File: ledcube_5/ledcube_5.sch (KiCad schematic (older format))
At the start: 60 parts, among them Q1 PN2222A, Q2 PN2222A, Q3 PN2222A, Q4 PN2222A, Q5 PN2222A, U1 74HC595, U2 74HC595, U3 74HC595, U4 74HC595, U5 FE310-G000

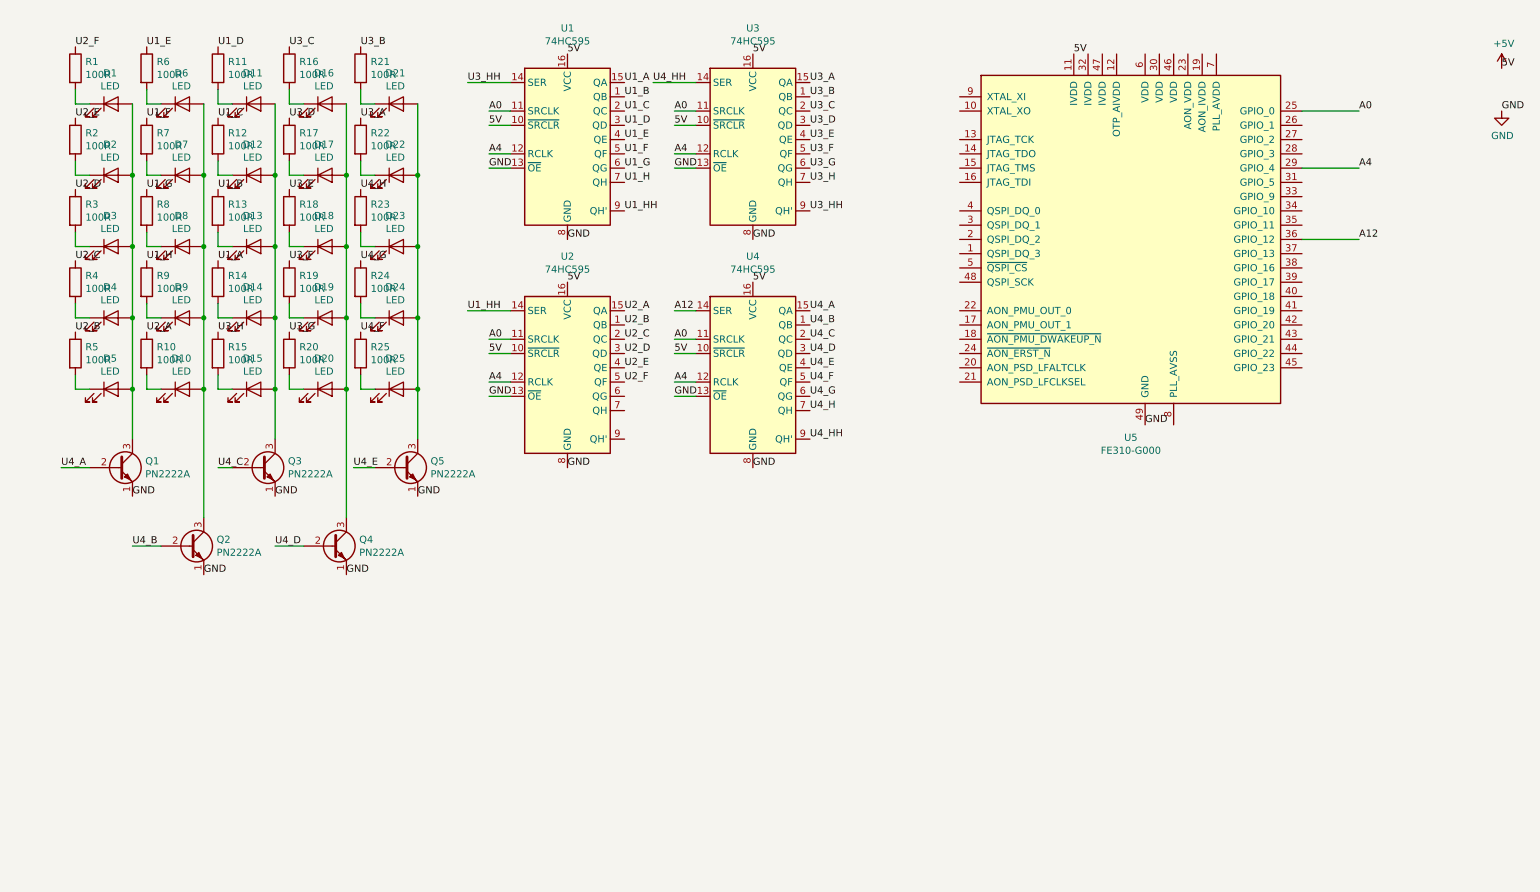
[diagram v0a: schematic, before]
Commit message: add power source
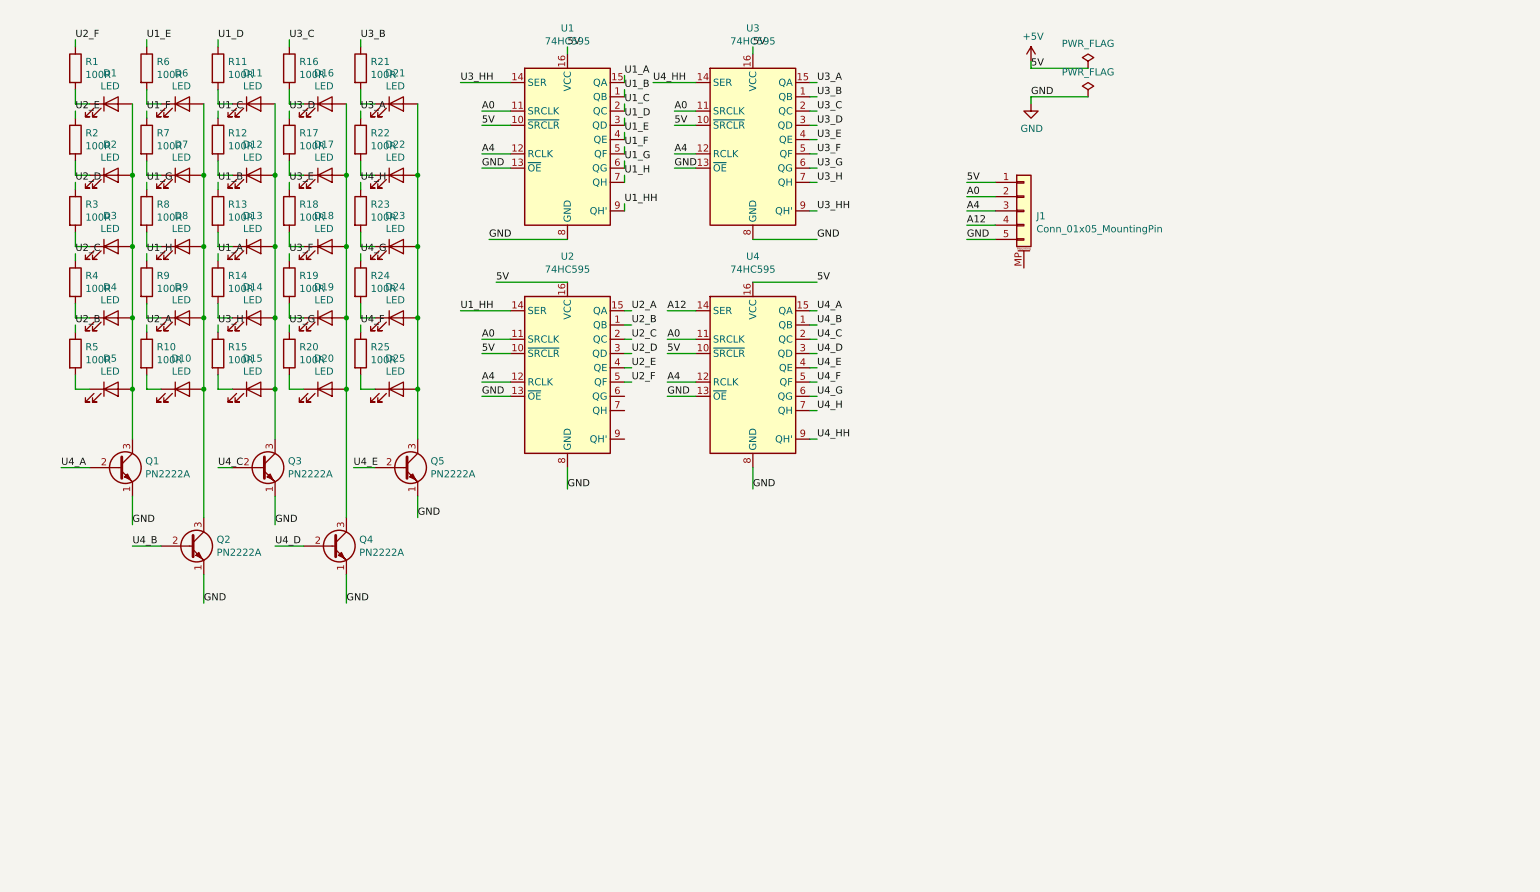
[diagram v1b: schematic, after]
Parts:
- removed U5: FE310-G000, Package_DFN_QFN:QFN-48-1EP_6x6mm_P0.4mm_EP4.2x4.2mm_ThermalVias, symbol MCU_SiFive:FE310-G000
- added J1: Conn_01x05_MountingPin, Connector_PinHeader_1.00mm:PinHeader_1x05_P1.00mm_Vertical, symbol Connector_Generic_MountingPin:Conn_01x05_MountingPin
- D1, D10, D11, D12, D13, D14, D15, D16, D17, D18, D19, D2, D20, D21, D22, D23, D24, D25, D3, D4, D5, D6, D7, D8, D9: footprint (none) -> Connector_Pin:Pin_D1.0mm_L10.0mm
- R1, R10, R11, R12, R13, R14, R15, R16, R17, R18, R19, R2, R20, R21, R22, R23, R24, R25, R3, R4, R5, R6, R7, R8, R9: footprint (none) -> Resistor_THT:R_Axial_DIN0411_L9.9mm_D3.6mm_P12.70mm_Horizontal
- U1, U2, U3, U4: footprint (none) -> Package_DIP:DIP-16_W7.62mm
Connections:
- net +5V: now also J1.1 (Pin_1)
- net A0: now also J1.2 (Pin_2)
- net A12: now also J1.4 (Pin_4)
- net A4: now also J1.3 (Pin_3)
- net GND: now also J1.5 (Pin_5)

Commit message: ledcube pcb draft
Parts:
- R1, R10, R11, R12, R13, R14, R15, R16, R17, R18, R19, R2, R20, R21, R22, R23, R24, R25, R3, R4, R5, R6, R7, R8, R9: footprint Resistor_THT:R_Axial_DIN0411_L9.9mm_D3.6mm_P12.70mm_Horizontal -> Resistor_THT:R_Axial_DIN0207_L6.3mm_D2.5mm_P10.16mm_Horizontal
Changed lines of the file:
@@
 F 0 "R10" H 1570 3046 50  0000 L CNN
 F 1 "100R" H 1570 2955 50  0000 L CNN
-F 2 "Resistor_THT:R_Axial_DIN0411_L9.9mm_D3.6mm_P12.70mm_Horizontal" V 1430 3000 50  0001 C CNN
+F 2 "Resistor_THT:R_Axial_DIN0207_L6.3mm_D2.5mm_P10.16mm_Horizontal" V 1430 3000 50  0001 C CNN
 F 3 "~" H 1500 3000 50  0001 C CNN
 	1    1500 3000
@@
 F 0 "R5" H 1070 3046 50  0000 L CNN
 F 1 "100R" H 1070 2955 50  0000 L CNN
-F 2 "Resistor_THT:R_Axial_DIN0411_L9.9mm_D3.6mm_P12.70mm_Horizontal" V 930 3000 50  0001 C CNN
+F 2 "Resistor_THT:R_Axial_DIN0207_L6.3mm_D2.5mm_P10.16mm_Horizontal" V 930 3000 50  0001 C CNN
 F 3 "~" H 1000 3000 50  0001 C CNN
 	1    1000 3000
@@
 F 0 "R15" H 2070 3046 50  0000 L CNN
 F 1 "100R" H 2070 2955 50  0000 L CNN
-F 2 "Resistor_THT:R_Axial_DIN0411_L9.9mm_D3.6mm_P12.70mm_Horizontal" V 1930 3000 50  0001 C CNN
+F 2 "Resistor_THT:R_Axial_DIN0207_L6.3mm_D2.5mm_P10.16mm_Horizontal" V 1930 3000 50  0001 C CNN
 F 3 "~" H 2000 3000 50  0001 C CNN
 	1    2000 3000
@@
 F 0 "R20" H 2570 3046 50  0000 L CNN
 F 1 "100R" H 2570 2955 50  0000 L CNN
-F 2 "Resistor_THT:R_Axial_DIN0411_L9.9mm_D3.6mm_P12.70mm_Horizontal" V 2430 3000 50  0001 C CNN
+F 2 "Resistor_THT:R_Axial_DIN0207_L6.3mm_D2.5mm_P10.16mm_Horizontal" V 2430 3000 50  0001 C CNN
 F 3 "~" H 2500 3000 50  0001 C CNN
 	1    2500 3000
@@
 F 0 "R14" H 2070 2546 50  0000 L CNN
 F 1 "100R" H 2070 2455 50  0000 L CNN
-F 2 "Resistor_THT:R_Axial_DIN0411_L9.9mm_D3.6mm_P12.70mm_Horizontal" V 1930 2500 50  0001 C CNN
+F 2 "Resistor_THT:R_Axial_DIN0207_L6.3mm_D2.5mm_P10.16mm_Horizontal" V 1930 2500 50  0001 C CNN
 F 3 "~" H 2000 2500 50  0001 C CNN
 	1    2000 2500
@@
 F 0 "R4" H 1070 2546 50  0000 L CNN
 F 1 "100R" H 1070 2455 50  0000 L CNN
-F 2 "Resistor_THT:R_Axial_DIN0411_L9.9mm_D3.6mm_P12.70mm_Horizontal" V 930 2500 50  0001 C CNN
+F 2 "Resistor_THT:R_Axial_DIN0207_L6.3mm_D2.5mm_P10.16mm_Horizontal" V 930 2500 50  0001 C CNN
 F 3 "~" H 1000 2500 50  0001 C CNN
 	1    1000 2500
@@
 F 0 "R9" H 1570 2546 50  0000 L CNN
 F 1 "100R" H 1570 2455 50  0000 L CNN
-F 2 "Resistor_THT:R_Axial_DIN0411_L9.9mm_D3.6mm_P12.70mm_Horizontal" V 1430 2500 50  0001 C CNN
+F 2 "Resistor_THT:R_Axial_DIN0207_L6.3mm_D2.5mm_P10.16mm_Horizontal" V 1430 2500 50  0001 C CNN
 F 3 "~" H 1500 2500 50  0001 C CNN
 	1    1500 2500
@@
 F 0 "R19" H 2570 2546 50  0000 L CNN
 F 1 "100R" H 2570 2455 50  0000 L CNN
-F 2 "Resistor_THT:R_Axial_DIN0411_L9.9mm_D3.6mm_P12.70mm_Horizontal" V 2430 2500 50  0001 C CNN
+F 2 "Resistor_THT:R_Axial_DIN0207_L6.3mm_D2.5mm_P10.16mm_Horizontal" V 2430 2500 50  0001 C CNN
 F 3 "~" H 2500 2500 50  0001 C CNN
 	1    2500 2500
@@
 F 0 "R24" H 3070 2546 50  0000 L CNN
 F 1 "100R" H 3070 2455 50  0000 L CNN
-F 2 "Resistor_THT:R_Axial_DIN0411_L9.9mm_D3.6mm_P12.70mm_Horizontal" V 2930 2500 50  0001 C CNN
+F 2 "Resistor_THT:R_Axial_DIN0207_L6.3mm_D2.5mm_P10.16mm_Horizontal" V 2930 2500 50  0001 C CNN
 F 3 "~" H 3000 2500 50  0001 C CNN
 	1    3000 2500
@@
 F 0 "R25" H 3070 3046 50  0000 L CNN
 F 1 "100R" H 3070 2955 50  0000 L CNN
-F 2 "Resistor_THT:R_Axial_DIN0411_L9.9mm_D3.6mm_P12.70mm_Horizontal" V 2930 3000 50  0001 C CNN
+F 2 "Resistor_THT:R_Axial_DIN0207_L6.3mm_D2.5mm_P10.16mm_Horizontal" V 2930 3000 50  0001 C CNN
 F 3 "~" H 3000 3000 50  0001 C CNN
 	1    3000 3000
@@
 F 0 "R3" H 1070 2046 50  0000 L CNN
 F 1 "100R" H 1070 1955 50  0000 L CNN
-F 2 "Resistor_THT:R_Axial_DIN0411_L9.9mm_D3.6mm_P12.70mm_Horizontal" V 930 2000 50  0001 C CNN
+F 2 "Resistor_THT:R_Axial_DIN0207_L6.3mm_D2.5mm_P10.16mm_Horizontal" V 930 2000 50  0001 C CNN
 F 3 "~" H 1000 2000 50  0001 C CNN
 	1    1000 2000
@@
 F 0 "R8" H 1570 2046 50  0000 L CNN
 F 1 "100R" H 1570 1955 50  0000 L CNN
-F 2 "Resistor_THT:R_Axial_DIN0411_L9.9mm_D3.6mm_P12.70mm_Horizontal" V 1430 2000 50  0001 C CNN
+F 2 "Resistor_THT:R_Axial_DIN0207_L6.3mm_D2.5mm_P10.16mm_Horizontal" V 1430 2000 50  0001 C CNN
 F 3 "~" H 1500 2000 50  0001 C CNN
 	1    1500 2000
@@
 F 0 "R13" H 2070 2046 50  0000 L CNN
 F 1 "100R" H 2070 1955 50  0000 L CNN
-F 2 "Resistor_THT:R_Axial_DIN0411_L9.9mm_D3.6mm_P12.70mm_Horizontal" V 1930 2000 50  0001 C CNN
+F 2 "Resistor_THT:R_Axial_DIN0207_L6.3mm_D2.5mm_P10.16mm_Horizontal" V 1930 2000 50  0001 C CNN
 F 3 "~" H 2000 2000 50  0001 C CNN
 	1    2000 2000
@@
 F 0 "R18" H 2570 2046 50  0000 L CNN
 F 1 "100R" H 2570 1955 50  0000 L CNN
-F 2 "Resistor_THT:R_Axial_DIN0411_L9.9mm_D3.6mm_P12.70mm_Horizontal" V 2430 2000 50  0001 C CNN
+F 2 "Resistor_THT:R_Axial_DIN0207_L6.3mm_D2.5mm_P10.16mm_Horizontal" V 2430 2000 50  0001 C CNN
 F 3 "~" H 2500 2000 50  0001 C CNN
 	1    2500 2000
@@
 F 0 "R23" H 3070 2046 50  0000 L CNN
 F 1 "100R" H 3070 1955 50  0000 L CNN
-F 2 "Resistor_THT:R_Axial_DIN0411_L9.9mm_D3.6mm_P12.70mm_Horizontal" V 2930 2000 50  0001 C CNN
+F 2 "Resistor_THT:R_Axial_DIN0207_L6.3mm_D2.5mm_P10.16mm_Horizontal" V 2930 2000 50  0001 C CNN
 F 3 "~" H 3000 2000 50  0001 C CNN
 	1    3000 2000
@@
 F 0 "R22" H 3070 1546 50  0000 L CNN
 F 1 "100R" H 3070 1455 50  0000 L CNN
-F 2 "Resistor_THT:R_Axial_DIN0411_L9.9mm_D3.6mm_P12.70mm_Horizontal" V 2930 1500 50  0001 C CNN
+F 2 "Resistor_THT:R_Axial_DIN0207_L6.3mm_D2.5mm_P10.16mm_Horizontal" V 2930 1500 50  0001 C CNN
 F 3 "~" H 3000 1500 50  0001 C CNN
 	1    3000 1500
@@
 F 0 "R17" H 2570 1546 50  0000 L CNN
 F 1 "100R" H 2570 1455 50  0000 L CNN
-F 2 "Resistor_THT:R_Axial_DIN0411_L9.9mm_D3.6mm_P12.70mm_Horizontal" V 2430 1500 50  0001 C CNN
+F 2 "Resistor_THT:R_Axial_DIN0207_L6.3mm_D2.5mm_P10.16mm_Horizontal" V 2430 1500 50  0001 C CNN
 F 3 "~" H 2500 1500 50  0001 C CNN
 	1    2500 1500
@@
 F 0 "R12" H 2070 1546 50  0000 L CNN
 F 1 "100R" H 2070 1455 50  0000 L CNN
-F 2 "Resistor_THT:R_Axial_DIN0411_L9.9mm_D3.6mm_P12.70mm_Horizontal" V 1930 1500 50  0001 C CNN
+F 2 "Resistor_THT:R_Axial_DIN0207_L6.3mm_D2.5mm_P10.16mm_Horizontal" V 1930 1500 50  0001 C CNN
 F 3 "~" H 2000 1500 50  0001 C CNN
 	1    2000 1500
@@
 F 0 "R7" H 1570 1546 50  0000 L CNN
 F 1 "100R" H 1570 1455 50  0000 L CNN
-F 2 "Resistor_THT:R_Axial_DIN0411_L9.9mm_D3.6mm_P12.70mm_Horizontal" V 1430 1500 50  0001 C CNN
+F 2 "Resistor_THT:R_Axial_DIN0207_L6.3mm_D2.5mm_P10.16mm_Horizontal" V 1430 1500 50  0001 C CNN
 F 3 "~" H 1500 1500 50  0001 C CNN
 	1    1500 1500
@@
 F 0 "R2" H 1070 1546 50  0000 L CNN
 F 1 "100R" H 1070 1455 50  0000 L CNN
-F 2 "Resistor_THT:R_Axial_DIN0411_L9.9mm_D3.6mm_P12.70mm_Horizontal" V 930 1500 50  0001 C CNN
+F 2 "Resistor_THT:R_Axial_DIN0207_L6.3mm_D2.5mm_P10.16mm_Horizontal" V 930 1500 50  0001 C CNN
 F 3 "~" H 1000 1500 50  0001 C CNN
 	1    1000 1500
@@
 F 0 "R1" H 1070 1046 50  0000 L CNN
 F 1 "100R" H 1070 955 50  0000 L CNN
-F 2 "Resistor_THT:R_Axial_DIN0411_L9.9mm_D3.6mm_P12.70mm_Horizontal" V 930 1000 50  0001 C CNN
+F 2 "Resistor_THT:R_Axial_DIN0207_L6.3mm_D2.5mm_P10.16mm_Horizontal" V 930 1000 50  0001 C CNN
 F 3 "~" H 1000 1000 50  0001 C CNN
 	1    1000 1000
@@
 F 0 "R6" H 1570 1046 50  0000 L CNN
 F 1 "100R" H 1570 955 50  0000 L CNN
-F 2 "Resistor_THT:R_Axial_DIN0411_L9.9mm_D3.6mm_P12.70mm_Horizontal" V 1430 1000 50  0001 C CNN
+F 2 "Resistor_THT:R_Axial_DIN0207_L6.3mm_D2.5mm_P10.16mm_Horizontal" V 1430 1000 50  0001 C CNN
 F 3 "~" H 1500 1000 50  0001 C CNN
 	1    1500 1000
@@
 F 0 "R11" H 2070 1046 50  0000 L CNN
 F 1 "100R" H 2070 955 50  0000 L CNN
-F 2 "Resistor_THT:R_Axial_DIN0411_L9.9mm_D3.6mm_P12.70mm_Horizontal" V 1930 1000 50  0001 C CNN
+F 2 "Resistor_THT:R_Axial_DIN0207_L6.3mm_D2.5mm_P10.16mm_Horizontal" V 1930 1000 50  0001 C CNN
 F 3 "~" H 2000 1000 50  0001 C CNN
 	1    2000 1000
@@
 F 0 "R16" H 2570 1046 50  0000 L CNN
 F 1 "100R" H 2570 955 50  0000 L CNN
-F 2 "Resistor_THT:R_Axial_DIN0411_L9.9mm_D3.6mm_P12.70mm_Horizontal" V 2430 1000 50  0001 C CNN
+F 2 "Resistor_THT:R_Axial_DIN0207_L6.3mm_D2.5mm_P10.16mm_Horizontal" V 2430 1000 50  0001 C CNN
 F 3 "~" H 2500 1000 50  0001 C CNN
 	1    2500 1000
@@
 F 0 "R21" H 3070 1046 50  0000 L CNN
 F 1 "100R" H 3070 955 50  0000 L CNN
-F 2 "Resistor_THT:R_Axial_DIN0411_L9.9mm_D3.6mm_P12.70mm_Horizontal" V 2930 1000 50  0001 C CNN
+F 2 "Resistor_THT:R_Axial_DIN0207_L6.3mm_D2.5mm_P10.16mm_Horizontal" V 2930 1000 50  0001 C CNN
 F 3 "~" H 3000 1000 50  0001 C CNN
 	1    3000 1000

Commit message: ledcube pcb tracks
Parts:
- added J2, J3, J4, J5, J6: Conn_01x01, Connector_Pin:Pin_D1.0mm_L10.0mm, symbol Connector_Generic:Conn_01x01
- J1: footprint Connector_PinHeader_1.00mm:PinHeader_1x05_P1.00mm_Vertical -> Connector_PinHeader_2.00mm:PinHeader_1x05_P2.00mm_Vertical
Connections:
- net at D1.2 (A), D2.2 (A), D3.2 (A)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: no longer Q1.3 (C)
- net at D10.2 (A), D6.2 (A), D7.2 (A)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: no longer Q2.3 (C)
- net at D11.2 (A), D12.2 (A), D13.2 (A)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: no longer Q3.3 (C)
- net at D16.2 (A), D17.2 (A), D18.2 (A)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: no longer Q4.3 (C)
- net at D21.2 (A), D22.2 (A), D23.2 (A)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: no longer Q5.3 (C)
- new net: J4.1 (Pin_1), Q3.3 (C)
- new net: J3.1 (Pin_1), Q2.3 (C)
- new net: J2.1 (Pin_1), Q1.3 (C)
- new net: J5.1 (Pin_1), Q4.3 (C)
- new net: J6.1 (Pin_1), Q5.3 (C)
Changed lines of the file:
@@
 	1    0    0    -1
 $EndComp
-Wire Wire Line
-	1400 3250 1400 3600
-Connection ~ 1400 3250
-Wire Wire Line
-	1900 3250 1900 4150
-Connection ~ 1900 3250
-Wire Wire Line
-	2400 3250 2400 3600
-Connection ~ 2400 3250
-Wire Wire Line
-	2900 3250 2900 4150
-Connection ~ 2900 3250
-Wire Wire Line
-	3400 3250 3400 3600
-Connection ~ 3400 3250
 Text Label 7250 2100 0    50   ~ 0
 A12
@@
 F 0 "J1" H 7738 1964 50  0000 L CNN
 F 1 "Conn_01x05_MountingPin" H 7738 1873 50  0000 L CNN
-F 2 "Connector_PinHeader_1.00mm:PinHeader_1x05_P1.00mm_Vertical" H 7650 2000 50  0001 C CNN
+F 2 "Connector_PinHeader_2.00mm:PinHeader_1x05_P2.00mm_Vertical" H 7650 2000 50  0001 C CNN
 F 3 "~" H 7650 2000 50  0001 C CNN
 	1    7650 2000
@@
 	1    0    0    -1
 $EndComp
+$Comp
+L Connector_Generic:Conn_01x01 J2
+U 1 1 611412CA
+P 1600 3600
+F 0 "J2" H 1680 3642 50  0000 L CNN
+F 1 "Conn_01x01" H 1680 3551 50  0000 L CNN
+F 2 "Connector_Pin:Pin_D1.0mm_L10.0mm" H 1600 3600 50  0001 C CNN
+F 3 "~" H 1600 3600 50  0001 C CNN
+	1    1600 3600
+	1    0    0    -1
+$EndComp
+$Comp
+L Connector_Generic:Conn_01x01 J6
+U 1 1 611441A3
+P 3600 3600
+F 0 "J6" H 3680 3642 50  0000 L CNN
+F 1 "Conn_01x01" H 3680 3551 50  0000 L CNN
+F 2 "Connector_Pin:Pin_D1.0mm_L10.0mm" H 3600 3600 50  0001 C CNN
+F 3 "~" H 3600 3600 50  0001 C CNN
+	1    3600 3600
+	1    0    0    -1
+$EndComp
+$Comp
+L Connector_Generic:Conn_01x01 J5
+U 1 1 61143AA4
+P 3100 4150
+F 0 "J5" H 3180 4192 50  0000 L CNN
+F 1 "Conn_01x01" H 3180 4101 50  0000 L CNN
+F 2 "Connector_Pin:Pin_D1.0mm_L10.0mm" H 3100 4150 50  0001 C CNN
+F 3 "~" H 3100 4150 50  0001 C CNN
+	1    3100 4150
+	1    0    0    -1
+$EndComp
+$Comp
+L Connector_Generic:Conn_01x01 J3
+U 1 1 61142E71
+P 2100 4150
+F 0 "J3" H 2180 4192 50  0000 L CNN
+F 1 "Conn_01x01" H 2180 4101 50  0000 L CNN
+F 2 "Connector_Pin:Pin_D1.0mm_L10.0mm" H 2100 4150 50  0001 C CNN
+F 3 "~" H 2100 4150 50  0001 C CNN
+	1    2100 4150
+	1    0    0    -1
+$EndComp
+$Comp
+L Connector_Generic:Conn_01x01 J4
+U 1 1 61143492
+P 2600 3600
+F 0 "J4" H 2680 3642 50  0000 L CNN
+F 1 "Conn_01x01" H 2680 3551 50  0000 L CNN
+F 2 "Connector_Pin:Pin_D1.0mm_L10.0mm" H 2600 3600 50  0001 C CNN
+F 3 "~" H 2600 3600 50  0001 C CNN
+	1    2600 3600
+	1    0    0    -1
+$EndComp
